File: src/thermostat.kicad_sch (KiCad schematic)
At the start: 110 parts, among them U18 AD5680, U19 MAX1968xUI, U20 RS8552, U21 TLV9001IDCK, U22 AD7172-2, U23 AD7172-4BCPZ

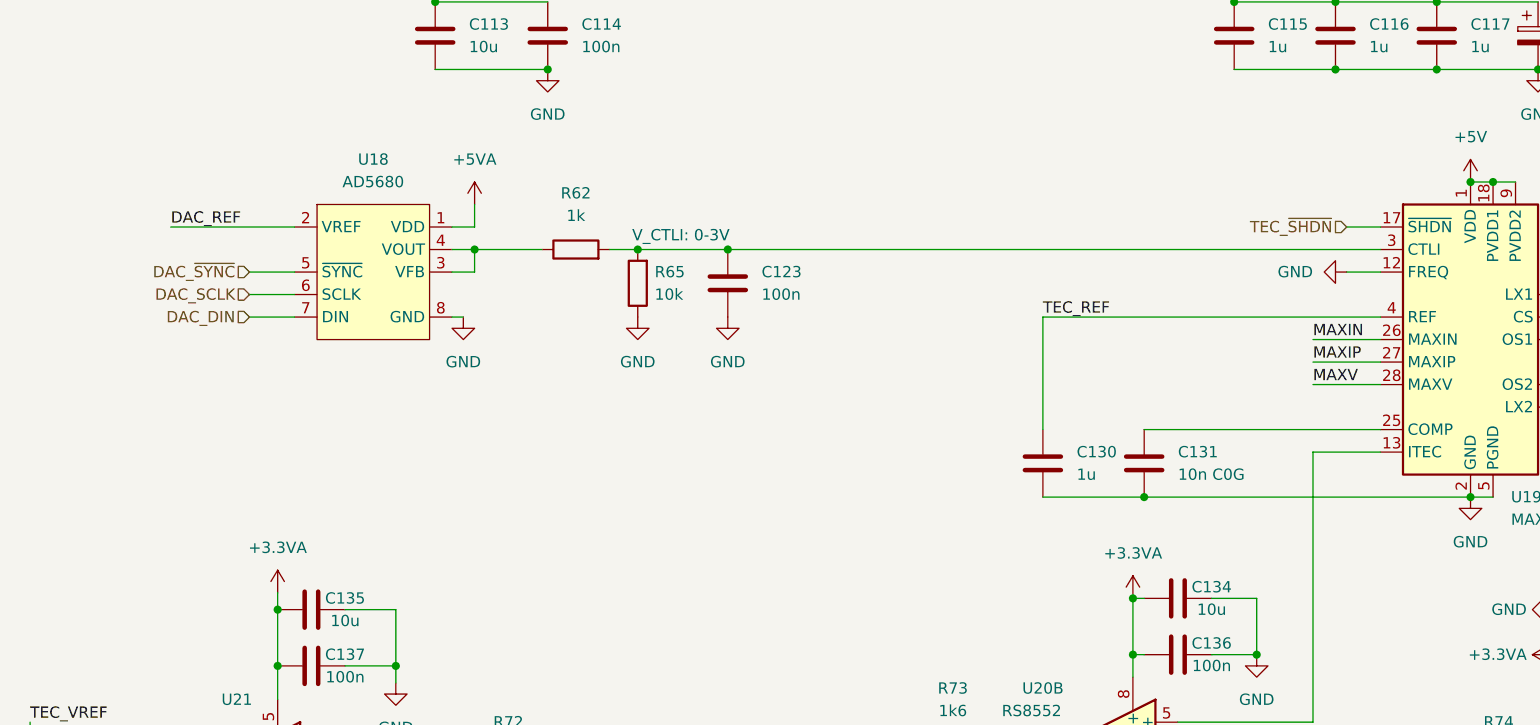
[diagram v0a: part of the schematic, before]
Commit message: sch, pcb: Add TDAC_VFB. Change 2u2 PMLCAP P/N - Connect TDAC voltage output through a RC LPF to MCU PC0(ADC123_IN10) - 2u2 PMLCAP P/N is changed to 16V version instead of 35V for lower cost
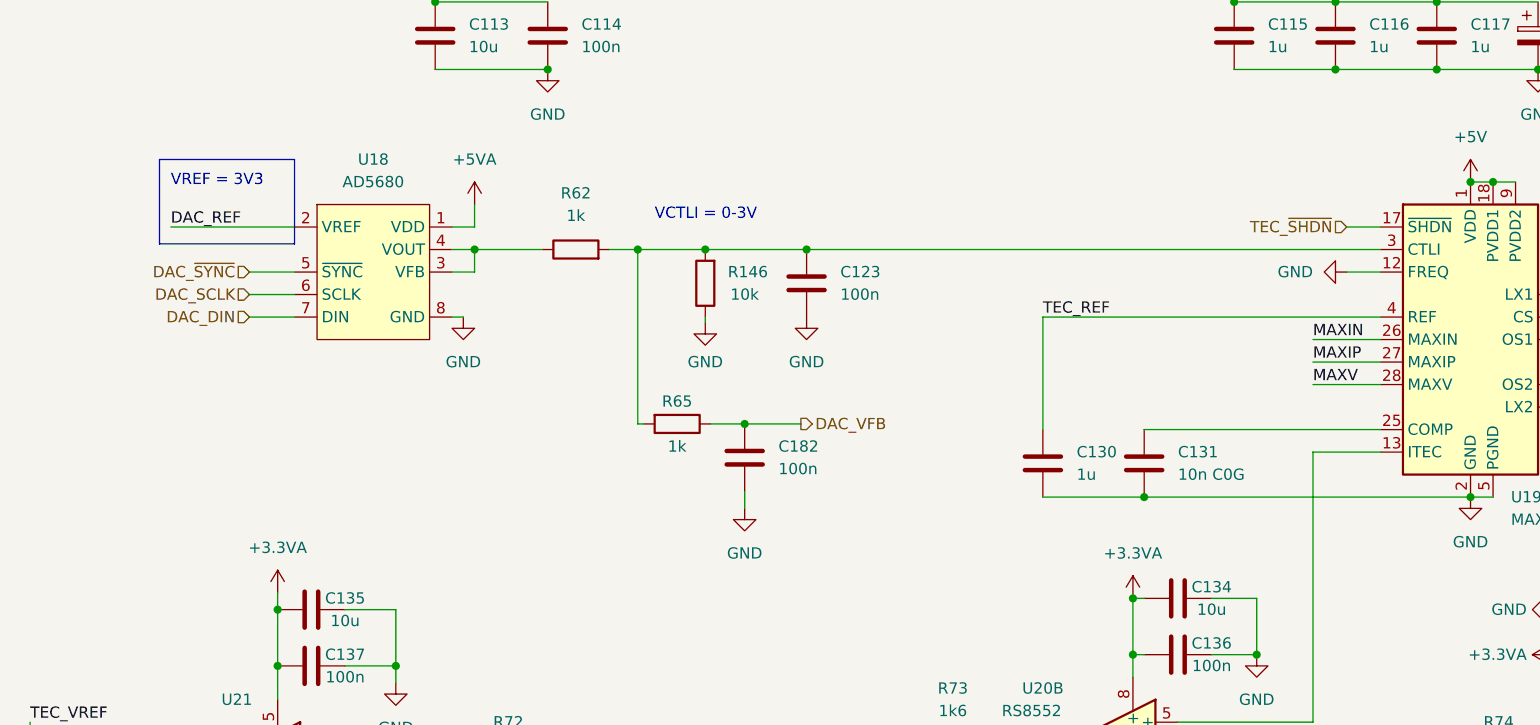
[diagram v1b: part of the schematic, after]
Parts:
- added C182: 100n, Capacitor_SMD:C_0603_1608Metric, symbol Device:C
- added R146: 10k, Resistor_SMD:R_0603_1608Metric, symbol Device:R
- R65: value 10k -> 1k; MFR_PN RNCP0603FTD10K0 -> RP0603BRD071KL; MFR_PN_ALT RMCF0603FT10K0 -> WR06X1001FTL
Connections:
- net GND: now also C182.2, R146.1; no longer R65.1
- net at C123.1, R62.2, R65.2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: now also R146.2
- new net DAC_VFB: C182.1, R65.1
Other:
- note added: "VCTLI = 0-3V"
- note added: "VREF = 3V3"
- note removed: "V_CTLI: 0-3V"
- moved on the sheet: C123

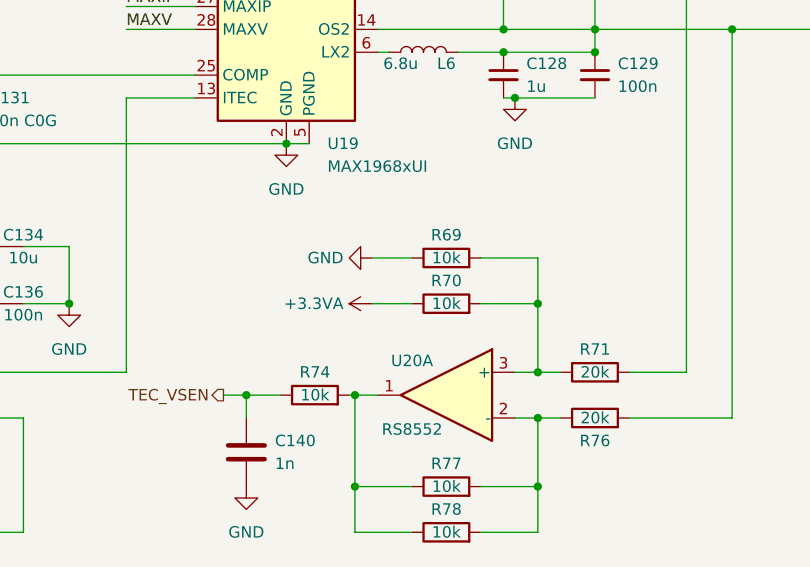
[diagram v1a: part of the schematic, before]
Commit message: sch, pcb: Add 0R to use TEC_VREF to bias TEC_VSEN - Optional
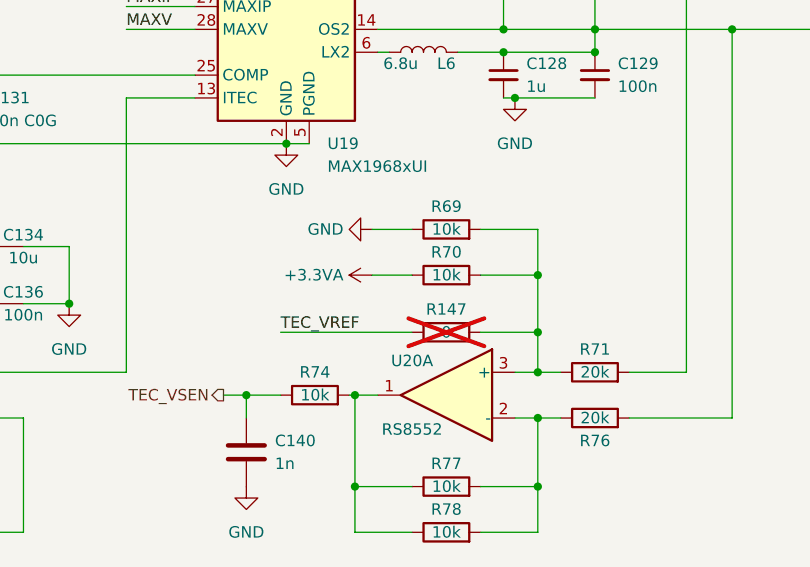
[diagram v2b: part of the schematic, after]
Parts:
- added R147: 0, Resistor_SMD:R_0603_1608Metric, symbol Device:R
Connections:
- net TEC_VREF: now also R147.2
- net at R69.2, R70.2, R71.1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: now also R147.1
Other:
- moved on the sheet: R69, R70
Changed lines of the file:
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@@
   (junction (at 53.34 245.745) (diameter 0) (color 0 0 0 0)
   )
+  (junction (at 328.93 140.335) (diameter 0) (color 0 0 0 0)
+  )
   (junction (at 161.29 208.915) (diameter 0) (color 0 0 0 0)
   )
@@
   (junction (at 278.765 196.215) (diameter 0) (color 0 0 0 0)
   )
-  (junction (at 328.93 137.16) (diameter 0) (color 0 0 0 0)
+  (junction (at 328.93 133.985) (diameter 0) (color 0 0 0 0)
   )
   (junction (at 96.52 93.98) (diameter 0) (color 0 0 0 0)
@@
     (stroke (width 0) (type default))
   )
+  (wire (pts (xy 300.355 140.335) (xy 314.96 140.335))
+    (stroke (width 0) (type default))
+  )
   (wire (pts (xy 274.32 63.5) (xy 285.75 63.5))
     (stroke (width 0) (type default))
@@
     (stroke (width 0) (type default))
   )
-  (wire (pts (xy 310.515 132.08) (xy 314.96 132.08))
+  (wire (pts (xy 310.515 128.905) (xy 314.96 128.905))
     (stroke (width 0) (type default))
   )
@@
     (stroke (width 0) (type default))
   )
+  (wire (pts (xy 328.93 140.335) (xy 328.93 144.78))
+    (stroke (width 0) (type default))
+  )
   (wire (pts (xy 311.15 101.6) (xy 345.44 101.6))
     (stroke (width 0) (type default))
@@
     (stroke (width 0) (type default))
   )
-  (wire (pts (xy 322.58 132.08) (xy 328.93 132.08))
+  (wire (pts (xy 322.58 128.905) (xy 328.93 128.905))
     (stroke (width 0) (type default))
   )
@@
     (stroke (width 0) (type default))
   )
-  (wire (pts (xy 328.93 137.16) (xy 328.93 144.78))
+  (wire (pts (xy 328.93 133.985) (xy 328.93 140.335))
     (stroke (width 0) (type default))
   )
@@
     (stroke (width 0) (type default))
   )
-  (wire (pts (xy 310.515 137.16) (xy 314.96 137.16))
+  (wire (pts (xy 310.515 133.985) (xy 314.96 133.985))
     (stroke (width 0) (type default))
   )
@@
     (stroke (width 0) (type default))
   )
-  (wire (pts (xy 322.58 137.16) (xy 328.93 137.16))
+  (wire (pts (xy 322.58 133.985) (xy 328.93 133.985))
     (stroke (width 0) (type default))
   )
@@
     (stroke (width 0) (type default))
   )
+  (wire (pts (xy 322.58 140.335) (xy 328.93 140.335))
+    (stroke (width 0) (type default))
+  )
   (wire (pts (xy 177.165 238.125) (xy 184.15 238.125))
     (stroke (width 0) (type default))
@@
     (stroke (width 0) (type default))
   )
-  (wire (pts (xy 328.93 132.08) (xy 328.93 137.16))
+  (wire (pts (xy 328.93 128.905) (xy 328.93 133.985))
     (stroke (width 0) (type default))
   )
@@
     (effects (font (size 1.27 1.27)) (justify left bottom))
   )
+  (label "TEC_VREF" (at 300.355 140.335 0) (fields_autoplaced)
+    (effects (font (size 1.27 1.27)) (justify left bottom))
+  )
   (label "TEC_REF" (at 252.73 99.06 0) (fields_autoplaced)
     (effects (font (size 1.27 1.27)) (justify left bottom))
@@
     )
   )
-  (symbol (lib_id "Device:R") (at 318.77 132.08 90) (unit 1)
+  (symbol (lib_id "Device:R") (at 318.77 128.905 90) (unit 1)
     (in_bom yes) (on_board yes) (dnp no)
-    (property "Reference" "R69" (at 318.77 129.54 90)
+    (property "Reference" "R69" (at 318.77 126.365 90)
       (effects (font (size 1.27 1.27)))
     )
-    (property "Value" "10k" (at 318.77 132.08 90)
+    (property "Value" "10k" (at 318.77 128.905 90)
       (effects (font (size 1.27 1.27)))
     )
-    (property "Footprint" "Resistor_SMD:R_0603_1608Metric" (at 318.77 133.858 90)
+    (property "Footprint" "Resistor_SMD:R_0603_1608Metric" (at 318.77 130.683 90)
       (effects (font (size 1.27 1.27)) hide)
     )
-    (property "Datasheet" "~" (at 318.77 132.08 0)
+    (property "Datasheet" "~" (at 318.77 128.905 0)
       (effects (font (size 1.27 1.27)) hide)
     )
-    (property "MFR_PN" "RNCP0603FTD10K0" (at 318.77 132.08 0)
+    (property "MFR_PN" "RNCP0603FTD10K0" (at 318.77 128.905 0)
       (effects (font (size 1.27 1.27)) hide)
     )
-    (property "MFR_PN_ALT" "RMCF0603FT10K0" (at 318.77 132.08 0)
+    (property "MFR_PN_ALT" "RMCF0603FT10K0" (at 318.77 128.905 0)
       (effects (font (size 1.27 1.27)) hide)
     )
@@
     )
   )
-  (symbol (lib_id "power:GND") (at 310.515 132.08 270) (unit 1)
+  (symbol (lib_id "power:GND") (at 310.515 128.905 270) (unit 1)
     (in_bom yes) (on_board yes) (dnp no) (fields_autoplaced)
-    (property "Reference" "#PWR0153" (at 304.165 132.08 0)
+    (property "Reference" "#PWR0153" (at 304.165 128.905 0)
       (effects (font (size 1.27 1.27)) hide)
     )
-    (property "Value" "GND" (at 307.34 132.08 90)
+    (property "Value" "GND" (at 307.34 128.905 90)
       (effects (font (size 1.27 1.27)) (justify right))
     )
-    (property "Footprint" "" (at 310.515 132.08 0)
+    (property "Footprint" "" (at 310.515 128.905 0)
       (effects (font (size 1.27 1.27)) hide)
     )
-    (property "Datasheet" "" (at 310.515 132.08 0)
+    (property "Datasheet" "" (at 310.515 128.905 0)
       (effects (font (size 1.27 1.27)) hide)
     )
@@
     )
   )
+  (symbol (lib_id "Device:R") (at 318.77 140.335 270) (unit 1)
+    (in_bom yes) (on_board yes) (dnp yes)
+    (property "Reference" "R147" (at 318.77 137.795 90)
+      (effects (font (size 1.27 1.27)))
+    )
+    (property "Value" "0" (at 318.77 140.335 90)
+      (effects (font (size 1.27 1.27)))
+    )
+    (property "Footprint" "Resistor_SMD:R_0603_1608Metric" (at 318.77 138.557 90)
+      (effects (font (size 1.27 1.27)) hide)
+    )
+    (property "Datasheet" "~" (at 318.77 140.335 0)
+      (effects (font (size 1.27 1.27)) hide)
+    )
+    (property "MFR_PN" "RMCF0603ZT0R00" (at 318.77 140.335 0)
+      (effects (font (size 1.27 1.27)) hide)
+    )
+    (property "MFR_PN_ALT" "CR0603-J/-000ELF" (at 318.77 140.335 0)
+      (effects (font (size 1.27 1.27)) hide)
+    )
+    (pin "1")
+    (pin "2")
+    (instances
+      (project "kirdy"
+        (path "/88da1dd8-9274-4b55-84fb-90006c9b6e8f/bda728c0-b189-4e05-8d4f-58a38acf883b"
+          (reference "R147") (unit 1)
+        )
+      )
+    )
+  )
   (symbol (lib_id "Device:R") (at 214.63 95.25 180) (unit 1)
     (in_bom yes) (on_board yes) (dnp no)
@@
     )
   )
-  (symbol (lib_id "Device:R") (at 318.77 137.16 90) (unit 1)
+  (symbol (lib_id "Device:R") (at 318.77 133.985 90) (unit 1)
     (in_bom yes) (on_board yes) (dnp no)
-    (property "Reference" "R70" (at 318.77 134.62 90)
+    (property "Reference" "R70" (at 318.77 131.445 90)
       (effects (font (size 1.27 1.27)))
     )
-    (property "Value" "10k" (at 318.77 137.16 90)
+    (property "Value" "10k" (at 318.77 133.985 90)
       (effects (font (size 1.27 1.27)))
     )
-    (property "Footprint" "Resistor_SMD:R_0603_1608Metric" (at 318.77 138.938 90)
+    (property "Footprint" "Resistor_SMD:R_0603_1608Metric" (at 318.77 135.763 90)
       (effects (font (size 1.27 1.27)) hide)
     )
-    (property "Datasheet" "~" (at 318.77 137.16 0)
+    (property "Datasheet" "~" (at 318.77 133.985 0)
       (effects (font (size 1.27 1.27)) hide)
     )
-    (property "MFR_PN" "RNCP0603FTD10K0" (at 318.77 137.16 0)
+    (property "MFR_PN" "RNCP0603FTD10K0" (at 318.77 133.985 0)
       (effects (font (size 1.27 1.27)) hide)
     )
-    (property "MFR_PN_ALT" "RMCF0603FT10K0" (at 318.77 137.16 0)
+    (property "MFR_PN_ALT" "RMCF0603FT10K0" (at 318.77 133.985 0)
       (effects (font (size 1.27 1.27)) hide)
     )
@@
     )
   )
-  (symbol (lib_id "power:+3.3VA") (at 310.515 137.16 90) (unit 1)
+  (symbol (lib_id "power:+3.3VA") (at 310.515 133.985 90) (unit 1)
     (in_bom yes) (on_board yes) (dnp no) (fields_autoplaced)
-    (property "Reference" "#PWR0157" (at 314.325 137.16 0)
+    (property "Reference" "#PWR0157" (at 314.325 133.985 0)
       (effects (font (size 1.27 1.27)) hide)
     )
-    (property "Value" "+3.3VA" (at 307.34 137.16 90)
+    (property "Value" "+3.3VA" (at 307.34 133.985 90)
       (effects (font (size 1.27 1.27)) (justify left))
     )
-    (property "Footprint" "" (at 310.515 137.16 0)
+    (property "Footprint" "" (at 310.515 133.985 0)
       (effects (font (size 1.27 1.27)) hide)
     )
-    (property "Datasheet" "" (at 310.515 137.16 0)
+    (property "Datasheet" "" (at 310.515 133.985 0)
       (effects (font (size 1.27 1.27)) hide)
     )

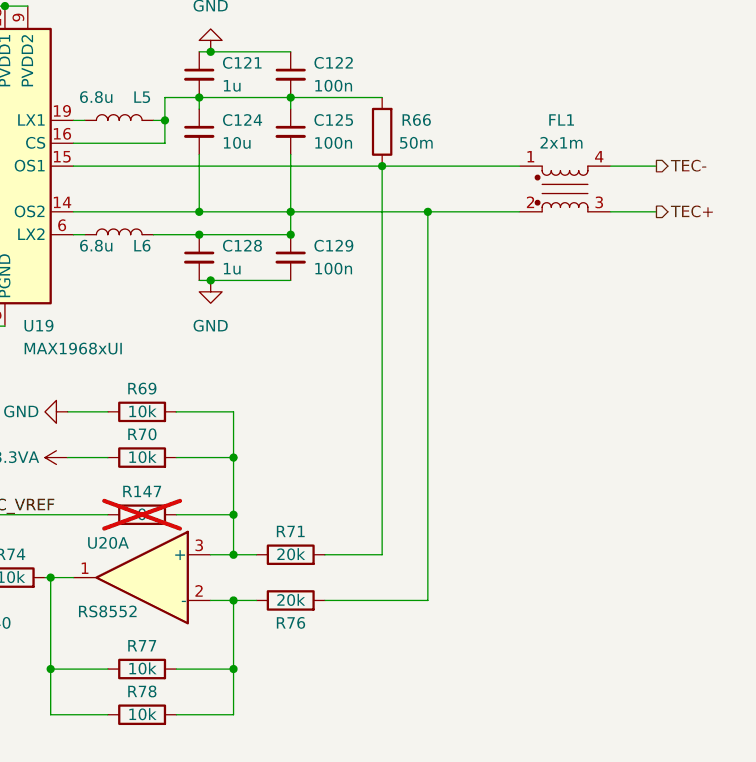
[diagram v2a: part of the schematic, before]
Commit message: sch, pcb: Correct opamp input polarity of TEC_VSEN - +ve IN connects to TEC+ - -ve IN  connects to TEC-
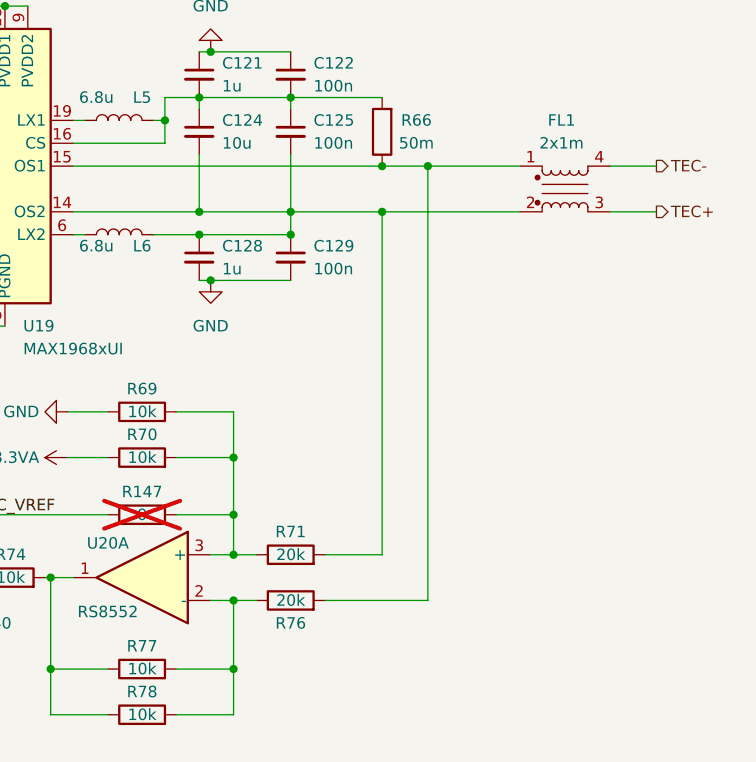
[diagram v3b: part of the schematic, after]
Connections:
- net at FL1.1, R66.1, U19.15 (OS1): now also R76.2; no longer R71.2
- net at C124.2, C125.2, C128.1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: now also R71.2; no longer R76.2
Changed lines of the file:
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@@
   (junction (at 267.97 188.595) (diameter 0) (color 0 0 0 0)
   )
-  (junction (at 350.52 106.68) (diameter 0) (color 0 0 0 0)
-  )
   (junction (at 297.18 63.5) (diameter 0) (color 0 0 0 0)
   )
@@
   (junction (at 214.63 91.44) (diameter 0) (color 0 0 0 0)
   )
+  (junction (at 350.52 101.6) (diameter 0) (color 0 0 0 0)
+  )
   (junction (at 149.225 149.86) (diameter 0) (color 0 0 0 0)
   )
@@
   )
   (junction (at 40.64 194.945) (diameter 0) (color 0 0 0 0)
+  )
+  (junction (at 345.44 106.68) (diameter 0) (color 0 0 0 0)
   )
   (junction (at 332.105 188.595) (diameter 0) (color 0 0 0 0)
@@
     (stroke (width 0) (type default))
   )
+  (wire (pts (xy 345.44 106.68) (xy 345.44 144.78))
+    (stroke (width 0) (type default))
+  )
   (wire (pts (xy 40.64 194.945) (xy 53.34 194.945))
     (stroke (width 0) (type default))
@@
     (stroke (width 0) (type default))
   )
+  (wire (pts (xy 350.52 101.6) (xy 350.52 149.86))
+    (stroke (width 0) (type default))
+  )
   (wire (pts (xy 80.01 253.365) (xy 92.71 253.365))
     (stroke (width 0) (type default))
@@
     (stroke (width 0) (type default))
   )
-  (wire (pts (xy 350.52 106.68) (xy 350.52 149.86))
-    (stroke (width 0) (type default))
-  )
   (wire (pts (xy 186.055 99.06) (xy 187.325 99.06))
     (stroke (width 0) (type default))
@@
     (stroke (width 0) (type default))
   )
-  (wire (pts (xy 345.44 101.6) (xy 345.44 144.78))
-    (stroke (width 0) (type default))
-  )
   (wire (pts (xy 326.39 144.78) (xy 328.93 144.78))
     (stroke (width 0) (type default))
@@
     (stroke (width 0) (type default))
   )
-  (wire (pts (xy 335.28 106.68) (xy 350.52 106.68))
+  (wire (pts (xy 335.28 106.68) (xy 345.44 106.68))
     (stroke (width 0) (type default))
   )
@@
     (stroke (width 0) (type default))
   )
+  (wire (pts (xy 350.52 101.6) (xy 360.68 101.6))
+    (stroke (width 0) (type default))
+  )
   (wire (pts (xy 267.335 188.595) (xy 267.97 188.595))
     (stroke (width 0) (type default))
   )
+  (wire (pts (xy 345.44 106.68) (xy 360.68 106.68))
+    (stroke (width 0) (type default))
+  )
   (wire (pts (xy 262.89 130.81) (xy 262.89 137.16))
     (stroke (width 0) (type default))
@@
     (stroke (width 0) (type default))
   )
-  (wire (pts (xy 350.52 106.68) (xy 360.68 106.68))
-    (stroke (width 0) (type default))
-  )
   (wire (pts (xy 297.815 188.595) (xy 307.975 188.595))
     (stroke (width 0) (type default))
@@
     (stroke (width 0) (type default))
   )
-  (wire (pts (xy 345.44 101.6) (xy 360.68 101.6))
-    (stroke (width 0) (type default))
-  )
+  (wire (pts (xy 345.44 101.6) (xy 350.52 101.6))
+    (stroke (width 0) (type default))
+  )

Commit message: sch: correct MFR/PNs for BSS138, TLV9001, TPS54620
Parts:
- U21: MFR_PN TLV9001QDBVRQ1 -> TLV9001IDCKR
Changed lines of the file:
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@@
       (effects (font (size 1.27 1.27)) hide)
     )
-    (property "MFR_PN" "TLV9001QDBVRQ1" (at 166.37 149.86 0)
+    (property "MFR_PN" "TLV9001IDCKR" (at 166.37 149.86 0)
       (effects (font (size 1.27 1.27)) hide)
     )
